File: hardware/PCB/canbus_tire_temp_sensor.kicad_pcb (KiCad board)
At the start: 2 copper layers, 40 x 20 mm, 42 parts, among them J1 TC2030, J2 2147210040, U1 TLE42744DV33ATMA1, U2 STM32F042K6Ux, U3 MLX90641ESF-BCA-000-SP, U4 TCAN3403DRQ1, Y1 ECS-160-10-36Q-AES-TR

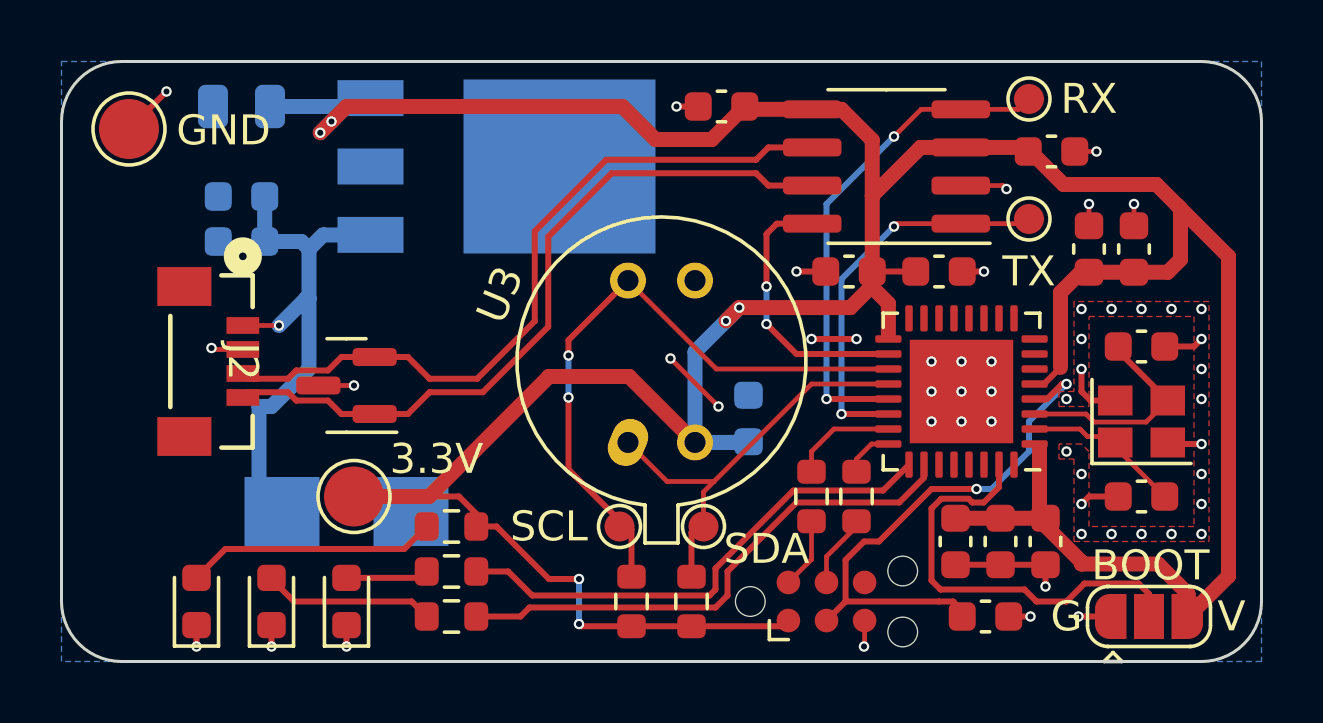
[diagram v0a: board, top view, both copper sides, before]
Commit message: version 1.2 - fixed IR sensor footprint
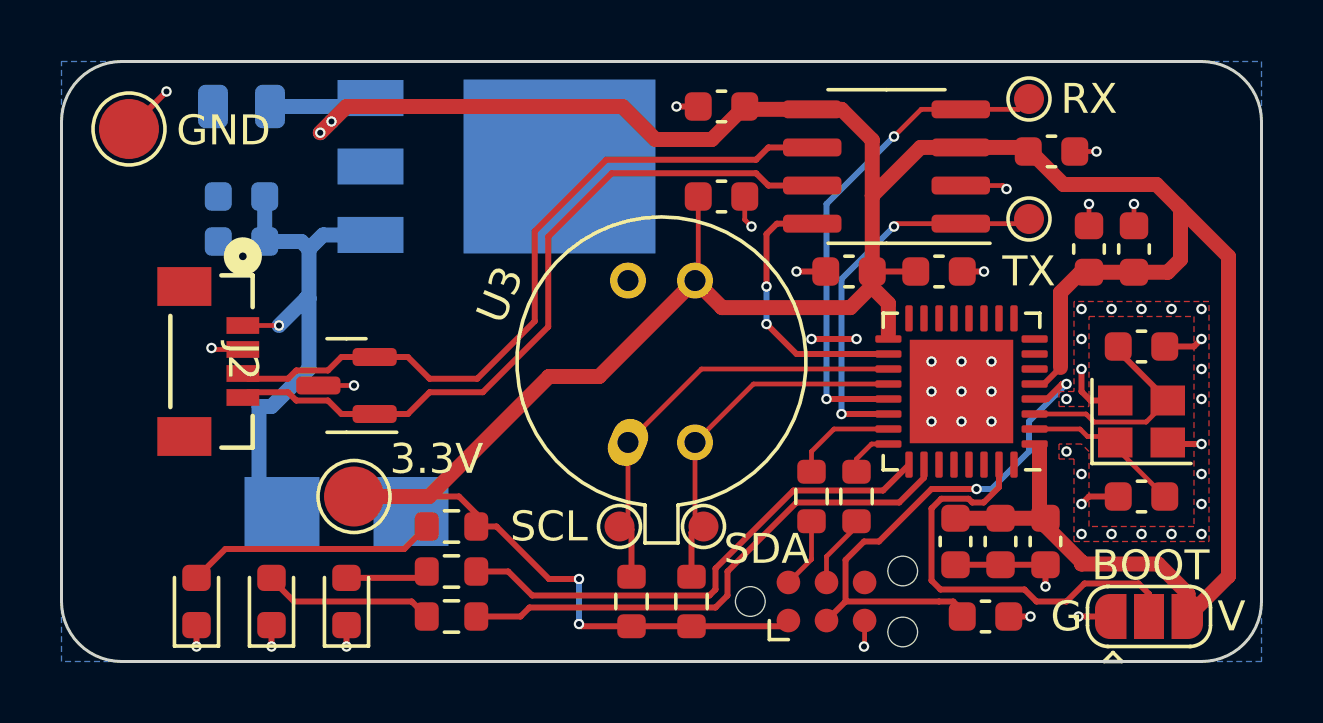
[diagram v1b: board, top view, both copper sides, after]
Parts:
- C14: moved to F.Cu
- moved C14 7.45 mm to (152.0, 94.5), turned to 180 degrees
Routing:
- net /SCL: track 21.6 -> 14.8 mm, vias 2 -> 0
- net +3V3: track 124.4 -> 122.0 mm, vias 6 -> 4
- net /SDA: track 14.2 -> 12.1 mm
- net GND: track 28.4 -> 27.2 mm, vias 52 -> 51

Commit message: V1.3 - Updated for cheaper JLCPCB options
Changed via size to most common
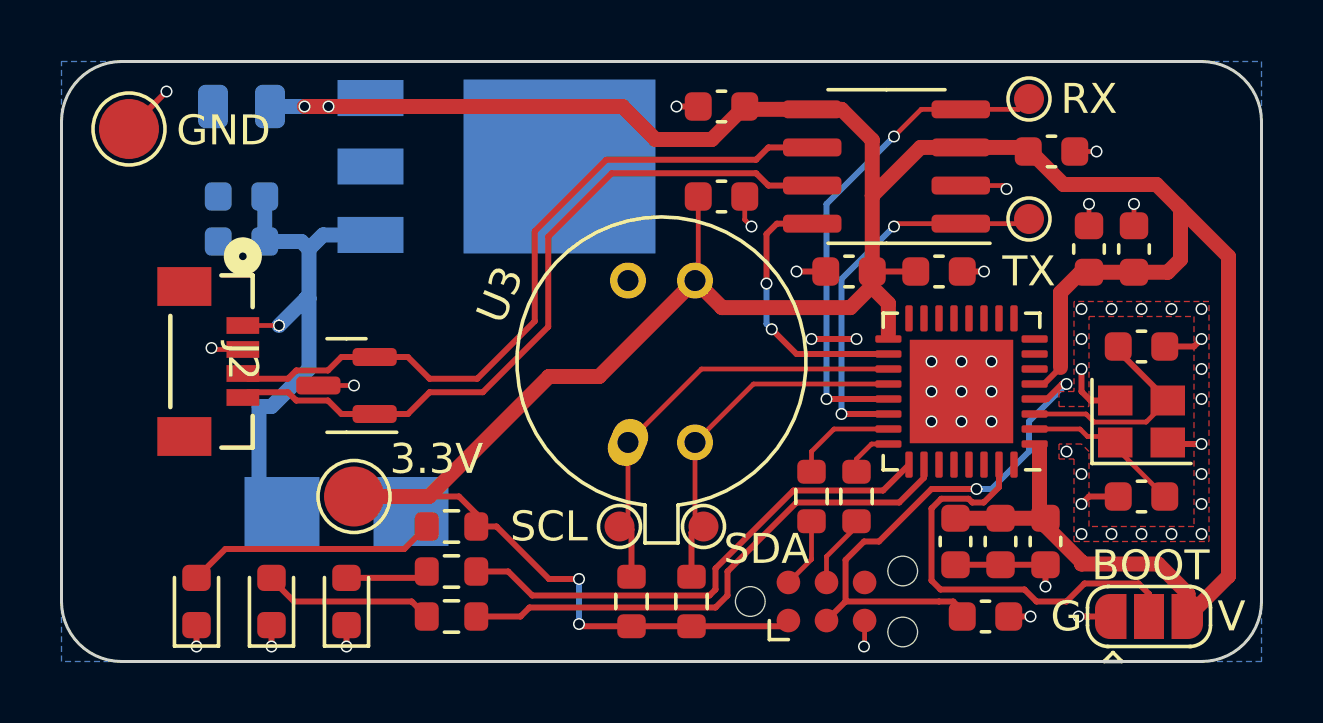
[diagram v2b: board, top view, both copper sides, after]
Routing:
- net GND: vias 51 -> 50
